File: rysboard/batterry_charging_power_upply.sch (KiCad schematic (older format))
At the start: 28 parts, among them J20 Conn_01x02, Q5 DMP3036SSD-13, Q6 DMP3036SSD-13, Q7 NST847BDP6T5G, Q9 Si7938DP-T1-GE3, U12 LTC4007

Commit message: more work done
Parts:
- removed C37, C40, C41, C42: C, symbol Device:C
- removed Q7: NST847BDP6T5G, Package_TO_SOT_SMD:SOT-963, symbol rysboard:NST847BDP6T5G
- removed R47, R48: R, symbol Device:R
- added C?: 15nF, Capacitor_SMD:C_0603_1608Metric, symbol Device:C
- added C? (x3): 10uF, Capacitor_SMD:C_1206_3216Metric, symbol Device:C
- added Q15: NST847BDP6T5G, Package_TO_SOT_SMD:SOT-963, symbol rysboard:DMP3036SSD-13
- added Q16: NST847BDP6T5G, Package_TO_SOT_SMD:SOT-963, symbol rysboard:NST847BDP6T5G
- added R41: 10KR, Resistor_SMD:R_0603_1608Metric_Pad1.05x0.95mm_HandSolder, symbol Device:R
- added R72: 10KR, Resistor_SMD:R_0603_1608Metric, symbol Device:R
- added R?: 26,7KR1%, Resistor_SMD:R_0603_1608Metric, symbol Device:R
- added R?: 25mR0.5%, symbol Device:R
- C35: value C -> 0.1uF; footprint (none) -> Capacitor_SMD:C_0603_1608Metric
- C38: value C -> 4,7nF; footprint (none) -> Capacitor_SMD:C_0603_1608Metric_Pad1.05x0.95mm_HandSolder
- C39: value C -> 10uF; footprint (none) -> Capacitor_SMD:C_1206_3216Metric
- L2: value INDUCTOR -> 10uH
- R39: value R -> 10KR; footprint (none) -> Resistor_SMD:R_0603_1608Metric_Pad1.05x0.95mm_HandSolder
- R42: value R -> 300KR; footprint (none) -> Resistor_SMD:R_0603_1608Metric_Pad1.05x0.95mm_HandSolder
- R46: value R -> 5KR; footprint (none) -> Resistor_SMD:R_0603_1608Metric_Pad1.05x0.95mm_HandSolder
- R49: value R -> 25mR0.5%
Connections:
- net +12V: now also C?.2, C?.2, C?.2, R?.1; no longer Q6.7 (d), Q6.8 (d), R46.1
- net +24V: now also Q15.1 (S1), R41.1; no longer C35.1, Q6.1 (S1), U12.1 (DCIN)
- net +BATT: now also C?.1
- net GND: now also C?.1, C?.1, C?.2, Q16.1 (E1), Q16.4 (E2), R?.1
- net current_monitor: now also R?.2
- net at R46.2, U12.18 (CLP): now also C?.1
- net at U12.24 (SHDN): now also Q16.3 (C2)
- net at R40.1: now also Q16.2 (B1)
- new net: C35.1, Q15.7 (d), Q15.8 (d), Q6.7 (d), Q6.8 (d), U12.1 (DCIN)
- new net: Q6.1 (S1), R46.1, R?.2
- new net: Q15.2 (G1), Q16.6 (C1), R41.2
- new net: Q16.5 (B2), R72.2
- new net ENABLE_CHARGING: R72.1
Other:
- note added: "SETUP FOR 4A"
- note added: "~2 Hours charging time"
- moved on the sheet: R40, R44

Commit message: more footprints
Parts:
- C34, C36: footprint (none) -> Capacitor_SMD:C_0603_1608Metric
- gave numbers to parts that had none: 6
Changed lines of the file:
@@
 F 0 "C36" H 6415 3646 50  0000 L CNN
 F 1 "C" H 6415 3555 50  0000 L CNN
-F 2 "" H 6338 3450 50  0001 C CNN
+F 2 "Capacitor_SMD:C_0603_1608Metric" H 6338 3450 50  0001 C CNN
 F 3 "~" H 6300 3600 50  0001 C CNN
 	1    6300 3600
@@
 F 0 "C34" H 2450 2400 50  0000 L CNN
 F 1 "C" H 2450 2250 50  0000 L CNN
-F 2 "" H 2638 2150 50  0001 C CNN
+F 2 "Capacitor_SMD:C_0603_1608Metric" H 2638 2150 50  0001 C CNN
 F 3 "~" H 2600 2300 50  0001 C CNN
 	1    2600 2300
@@
 Connection ~ 3650 2050
 $Comp
-L Device:C C?
+L Device:C C37
 U 1 1 6048E11B
 P 6850 2050
-F 0 "C?" H 6965 2096 50  0000 L CNN
+F 0 "C37" H 6965 2096 50  0000 L CNN
 F 1 "15nF" H 6965 2005 50  0000 L CNN
 F 2 "Capacitor_SMD:C_0603_1608Metric" H 6888 1900 50  0001 C CNN
@@
 	6850 2200 7550 2200
 $Comp
-L Device:C C?
+L Device:C C42
 U 1 1 6048ED93
 P 9650 2900
-F 0 "C?" H 9765 2946 50  0000 L CNN
+F 0 "C42" H 9765 2946 50  0000 L CNN
 F 1 "10uF" H 9765 2855 50  0000 L CNN
 F 2 "Capacitor_SMD:C_1206_3216Metric" H 9688 2750 50  0001 C CNN
@@
 ~2 Hours charging time
 $Comp
-L Device:R R?
+L Device:R R48
 U 1 1 6049324E
 P 7575 3600
-F 0 "R?" H 7575 3600 50  0000 C CNN
+F 0 "R48" H 7575 3600 50  0000 C CNN
 F 1 "26,7KR1%" H 7575 3800 50  0000 C CNN
 F 2 "Resistor_SMD:R_0603_1608Metric" V 7505 3600 50  0001 C CNN
@@
 	7575 3450 8325 3450
 $Comp
-L Device:R R?
+L Device:R R47
 U 1 1 604A0F07
 P 7550 2050
-F 0 "R?" H 7300 2000 50  0000 C CNN
+F 0 "R47" H 7300 2000 50  0000 C CNN
 F 1 "25mR0.5%" H 7275 1925 50  0000 C CNN
 F 2 "" V 7480 2050 50  0001 C CNN
@@
 Connection ~ 7550 1900
 $Comp
-L Device:C C?
+L Device:C C40
 U 1 1 604CA4CA
 P 8275 2050
-F 0 "C?" H 8390 2096 50  0000 L CNN
+F 0 "C40" H 8390 2096 50  0000 L CNN
 F 1 "10uF" H 8390 2005 50  0000 L CNN
 F 2 "Capacitor_SMD:C_1206_3216Metric" H 8313 1900 50  0001 C CNN
@@
 $EndComp
 $Comp
-L Device:C C?
+L Device:C C41
 U 1 1 604CA7A0
 P 8700 2050
-F 0 "C?" H 8815 2096 50  0000 L CNN
+F 0 "C41" H 8815 2096 50  0000 L CNN
 F 1 "10uF" H 8815 2005 50  0000 L CNN
 F 2 "Capacitor_SMD:C_1206_3216Metric" H 8738 1900 50  0001 C CNN
@@
 	9175 2200 9925 2200
 $Comp
-L power:GND #PWR?
+L power:GND #PWR0106
 U 1 1 604CDA85
 P 8700 1900
-F 0 "#PWR?" H 8700 1650 50  0001 C CNN
+F 0 "#PWR0106" H 8700 1650 50  0001 C CNN
 F 1 "GND" H 8705 1727 50  0000 C CNN
 F 2 "" H 8700 1900 50  0001 C CNN
@@
 $EndComp
 $Comp
-L power:GND #PWR?
+L power:GND #PWR0107
 U 1 1 604CE081
 P 8275 1900
-F 0 "#PWR?" H 8275 1650 50  0001 C CNN
+F 0 "#PWR0107" H 8275 1650 50  0001 C CNN
 F 1 "GND" H 8280 1727 50  0000 C CNN
 F 2 "" H 8275 1900 50  0001 C CNN

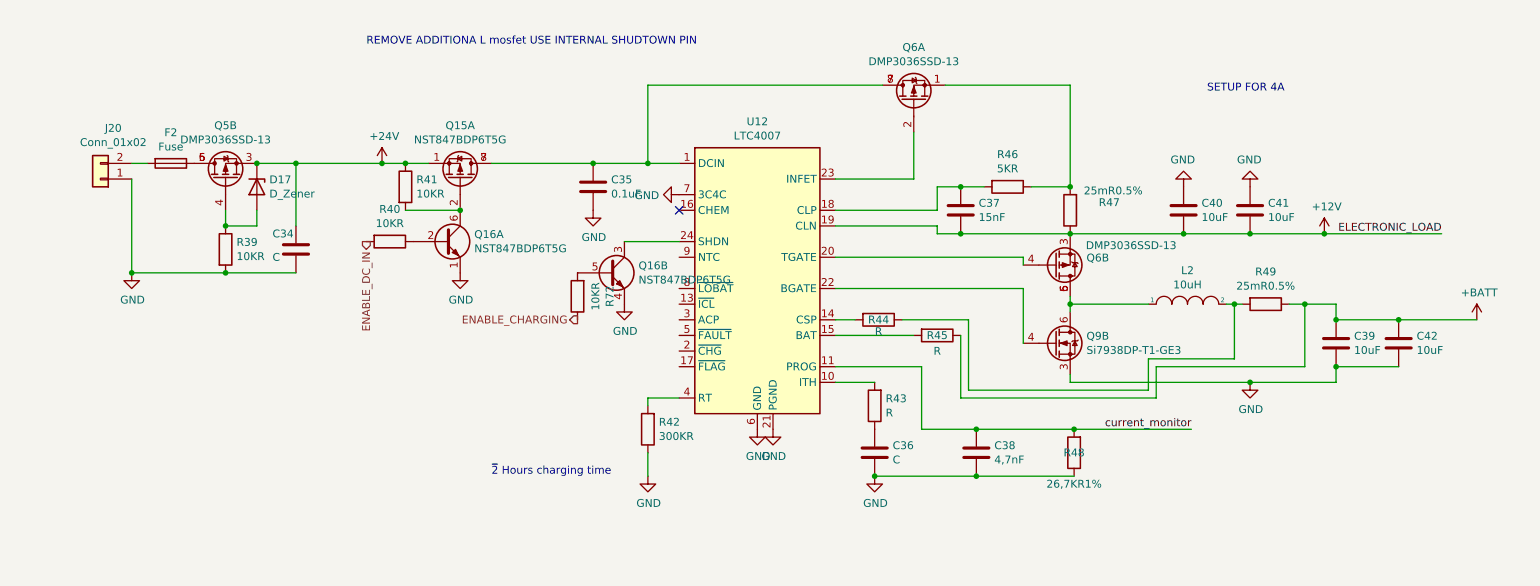
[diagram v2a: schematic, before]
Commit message: ltc4007 configured
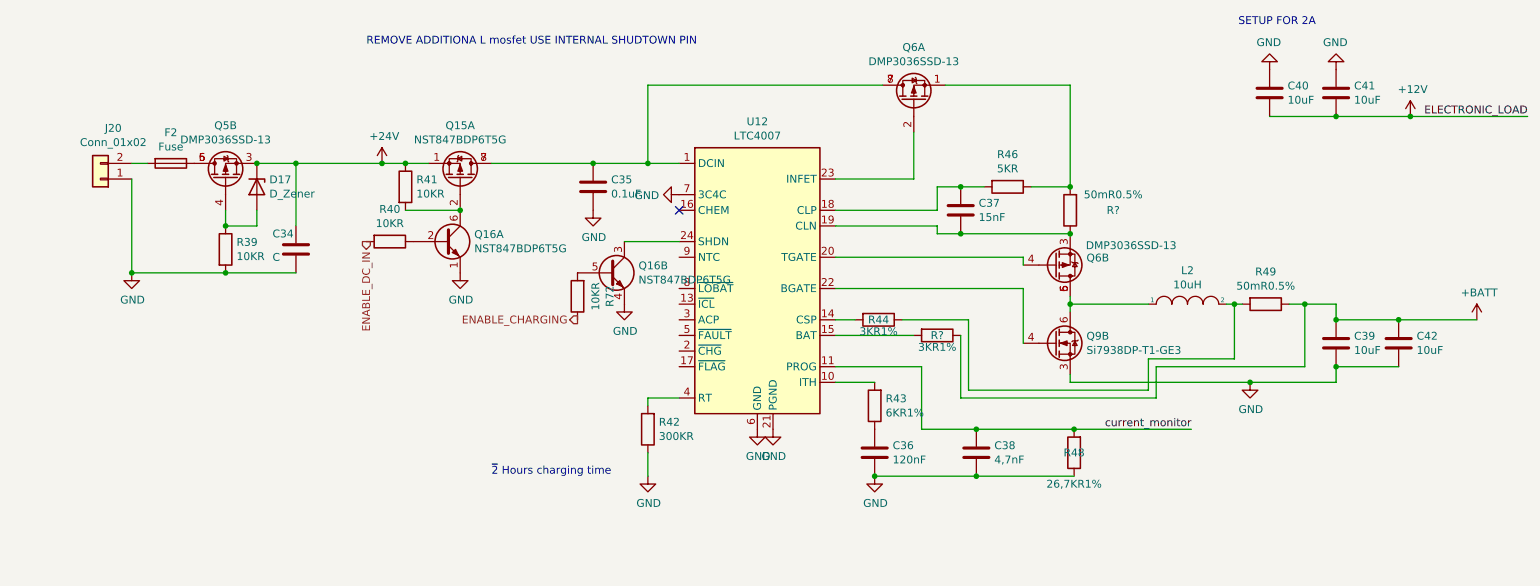
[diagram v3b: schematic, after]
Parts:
- removed R45: R, symbol Device:R
- removed R47: 25mR0.5%, symbol Device:R
- added R?: 3KR1%, Resistor_SMD:R_0603_1608Metric, symbol Device:R
- added R?: 50mR0.5%, symbol Device:R
- C36: value C -> 120nF
- R43: value R -> 6KR1%; footprint (none) -> Resistor_SMD:R_0603_1608Metric
- R44: value R -> 3KR1%; footprint (none) -> Resistor_SMD:R_0603_1608Metric
- R49: value 25mR0.5% -> 50mR0.5%
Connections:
- net +12V: no longer C37.2, Q6.3 (S2), U12.19 (CLN)
- net +BATT: now also R?.1
- net at U12.15 (BAT): now also R?.2
- net at Q6.1 (S1), R46.1: now also R?.2
- new net: C37.2, Q6.3 (S2), R?.1, U12.19 (CLN)
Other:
- note added: "SETUP FOR 2A"
- note removed: "SETUP FOR 4A"
- moved on the sheet: C40, C41

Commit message: LTC4007 done
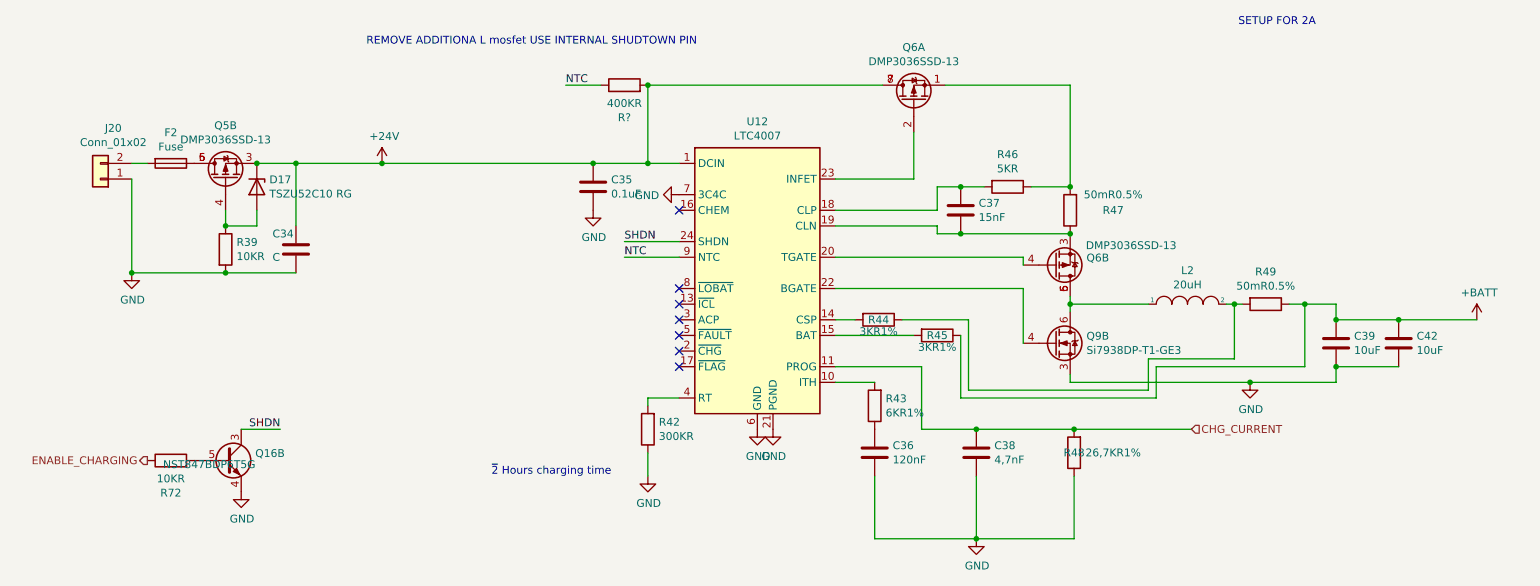
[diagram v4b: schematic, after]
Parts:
- removed C40, C41: 10uF, Capacitor_SMD:C_1206_3216Metric, symbol Device:C
- removed Q15: NST847BDP6T5G, Package_TO_SOT_SMD:SOT-963, symbol rysboard:DMP3036SSD-13
- removed unit 1 of Q16
- removed R40: 10KR, Resistor_SMD:R_0603_1608Metric, symbol Device:R
- removed R41: 10KR, Resistor_SMD:R_0603_1608Metric_Pad1.05x0.95mm_HandSolder, symbol Device:R
- added R?: 400KR, Resistor_SMD:R_0603_1608Metric, symbol Device:R
- D17: value D_Zener -> TSZU52C10 RG; footprint (none) -> Diode_SMD:D_0603_1608Metric
- F2: footprint (none) -> Fuse:Fuse_1206_3216Metric
- L2: value 10uH -> 20uH
- gave numbers to parts that had none: 2
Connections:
- net +24V: now also C35.1, Q6.7 (d), Q6.8 (d), U12.1 (DCIN), R?.2
- net SHDN: now reaches Q16.3 (C2), U12.24 (SHDN)
- net NTC: now reaches U12.9 (NTC)
- net NTC: now also R?.1
- net current_monitor renamed CHG_CURRENT
- no-connect marks 1 -> 7
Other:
- moved on the sheet: Q16B, R72
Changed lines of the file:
@@
 P 2350 1900
 F 0 "D17" V 2304 1980 50  0000 L CNN
-F 1 "D_Zener" V 2395 1980 50  0000 L CNN
-F 2 "" H 2350 1900 50  0001 C CNN
+F 1 "TSZU52C10 RG" V 2395 1980 50  0000 L CNN
+F 2 "Diode_SMD:D_0603_1608Metric" H 2350 1900 50  0001 C CNN
 F 3 "~" H 2350 1900 50  0001 C CNN
 	1    2350 1900
@@
 F 0 "F2" V 1603 1750 50  0000 C CNN
 F 1 "Fuse" V 1694 1750 50  0000 C CNN
-F 2 "" V 1730 1750 50  0001 C CNN
+F 2 "Fuse:Fuse_1206_3216Metric" V 1730 1750 50  0001 C CNN
 F 3 "~" H 1800 1750 50  0001 C CNN
 	1    1800 1750
@@
 P 8300 2650
 F 0 "L2" H 8300 2865 50  0000 C CNN
-F 1 "10uH" H 8300 2774 50  0000 C CNN
+F 1 "20uH" H 8300 2774 50  0000 C CNN
 F 2 "" H 8300 2650 50  0001 C CNN
 F 3 "~" H 8300 2650 50  0001 C CNN
@@
 $EndComp
 Wire Wire Line
-	6300 3750 6950 3750
-Connection ~ 6950 3750
-Wire Wire Line
 	6300 3150 6050 3150
 $Comp
 L power:GND #PWR046
 U 1 1 5FF27CDA
-P 6300 3750
-F 0 "#PWR046" H 6300 3500 50  0001 C CNN
-F 1 "GND" H 6305 3577 50  0000 C CNN
-F 2 "" H 6300 3750 50  0001 C CNN
-F 3 "" H 6300 3750 50  0001 C CNN
-	1    6300 3750
-	1    0    0    -1
-$EndComp
-Connection ~ 6300 3750
-Text Label 8325 3450 2    50   ~ 0
-current_monitor
-Text Label 10475 1450 2    50   ~ 0
-ELECTRONIC_LOAD
+P 6950 4150
+F 0 "#PWR046" H 6950 3900 50  0001 C CNN
+F 1 "GND" H 6955 3977 50  0000 C CNN
+F 2 "" H 6950 4150 50  0001 C CNN
+F 3 "" H 6950 4150 50  0001 C CNN
+	1    6950 4150
+	1    0    0    -1
+$EndComp
 $Comp
 L Device:R R42
@@
 REMOVE ADDITIONA L mosfet USE INTERNAL SHUDTOWN PIN
 $Comp
-L power:+12V #PWR061
-U 1 1 604387DC
-P 9725 1450
-F 0 "#PWR061" H 9725 1300 50  0001 C CNN
-F 1 "+12V" H 9740 1623 50  0000 C CNN
-F 2 "" H 9725 1450 50  0001 C CNN
-F 3 "" H 9725 1450 50  0001 C CNN
-	1    9725 1450
-	1    0    0    -1
-$EndComp
-$Comp
 L rysboard:DMP3036SSD-13 Q5
 U 2 1 6050A980
@@
 L Device:R R72
 U 1 1 6047C363
-P 4400 2600
-F 0 "R72" V 4193 2600 50  0000 C CNN
-F 1 "10KR" V 4284 2600 50  0000 C CNN
-F 2 "Resistor_SMD:R_0603_1608Metric" V 4330 2600 50  0001 C CNN
-F 3 "~" H 4400 2600 50  0001 C CNN
-	1    4400 2600
-	-1   0    0    1
+P 1800 3650
+F 0 "R72" V 1593 3650 50  0000 C CNN
+F 1 "10KR" V 1684 3650 50  0000 C CNN
+F 2 "Resistor_SMD:R_0603_1608Metric" V 1730 3650 50  0001 C CNN
+F 3 "~" H 1800 3650 50  0001 C CNN
+	1    1800 3650
+	0    -1   -1   0
 $EndComp
 $Comp
 L power:GND #PWR065
 U 1 1 6047C8D4
-P 4700 2650
-F 0 "#PWR065" H 4700 2400 50  0001 C CNN
-F 1 "GND" H 4705 2477 50  0000 C CNN
-F 2 "" H 4700 2650 50  0001 C CNN
-F 3 "" H 4700 2650 50  0001 C CNN
-	1    4700 2650
-	1    0    0    -1
-$EndComp
-Text HLabel 4400 2750 0    50   Output ~ 0
+P 2250 3850
+F 0 "#PWR065" H 2250 3600 50  0001 C CNN
+F 1 "GND" H 2255 3677 50  0000 C CNN
+F 2 "" H 2250 3850 50  0001 C CNN
+F 3 "" H 2250 3850 50  0001 C CNN
+	1    2250 3850
+	1    0    0    -1
+$EndComp
+Text HLabel 1650 3650 0    50   Output ~ 0
 ENABLE_CHARGING
 $Comp
 L rysboard:NST847BDP6T5G Q16
 U 2 1 6047E1C9
-P 4600 2450
-F 0 "Q16" H 4790 2496 50  0000 L CNN
-F 1 "NST847BDP6T5G" H 4790 2405 50  0000 L CNN
-F 2 "Package_TO_SOT_SMD:SOT-963" H 4800 2550 50  0001 C CNN
-F 3 "~" H 4600 2450 50  0001 C CNN
-	2    4600 2450
+P 2150 3650
+F 0 "Q16" H 2340 3696 50  0000 L CNN
+F 1 "NST847BDP6T5G" H 1750 3625 50  0000 L CNN
+F 2 "Package_TO_SOT_SMD:SOT-963" H 2350 3750 50  0001 C CNN
+F 3 "~" H 2150 3650 50  0001 C CNN
+	2    2150 3650
 	1    0    0    -1
 $EndComp
@@
 P 7575 3600
 F 0 "R48" H 7575 3600 50  0000 C CNN
-F 1 "26,7KR1%" H 7575 3800 50  0000 C CNN
+F 1 "26,7KR1%" H 7325 3600 50  0000 C CNN
 F 2 "Resistor_SMD:R_0603_1608Metric" V 7505 3600 50  0001 C CNN
 F 3 "~" H 7575 3600 50  0001 C CNN
@@
 $EndComp
 Wire Wire Line
-	6950 3750 7575 3750
-Wire Wire Line
 	6950 3450 7575 3450
 Connection ~ 7575 3450
 Wire Wire Line
 	7575 3450 8325 3450
-$Comp
-L Device:C C40
-U 1 1 604CA4CA
-P 8825 1300
-F 0 "C40" H 8940 1346 50  0000 L CNN
-F 1 "10uF" H 8940 1255 50  0000 L CNN
-F 2 "Capacitor_SMD:C_1206_3216Metric" H 8863 1150 50  0001 C CNN
-F 3 "~" H 8825 1300 50  0001 C CNN
-	1    8825 1300
-	1    0    0    -1
-$EndComp
-$Comp
-L Device:C C41
-U 1 1 604CA7A0
-P 9250 1300
-F 0 "C41" H 9365 1346 50  0000 L CNN
-F 1 "10uF" H 9365 1255 50  0000 L CNN
-F 2 "Capacitor_SMD:C_1206_3216Metric" H 9288 1150 50  0001 C CNN
-F 3 "~" H 9250 1300 50  0001 C CNN
-	1    9250 1300
-	1    0    0    -1
-$EndComp
-Wire Wire Line
-	8825 1450 9250 1450
-Connection ~ 9250 1450
-Wire Wire Line
-	9250 1450 9725 1450
-Connection ~ 9725 1450
-Wire Wire Line
-	9725 1450 10475 1450
-$Comp
-L power:GND #PWR0106
-U 1 1 604CDA85
-P 9250 1150
-F 0 "#PWR0106" H 9250 900 50  0001 C CNN
-F 1 "GND" H 9255 977 50  0000 C CNN
-F 2 "" H 9250 1150 50  0001 C CNN
-F 3 "" H 9250 1150 50  0001 C CNN
-	1    9250 1150
-	-1   0    0    1
-$EndComp
-$Comp
-L power:GND #PWR0107
-U 1 1 604CE081
-P 8825 1150
-F 0 "#PWR0107" H 8825 900 50  0001 C CNN
-F 1 "GND" H 8830 977 50  0000 C CNN
-F 2 "" H 8825 1150 50  0001 C CNN
-F 3 "" H 8825 1150 50  0001 C CNN
-	1    8825 1150
-	-1   0    0    1
-$EndComp
 Text Notes 8625 875  0    50   ~ 0
 SETUP FOR 2A
 $Comp
-L Device:R R?
+L Device:R R45
 U 1 1 60466C52
 P 6700 2850
-F 0 "R?" V 6700 2850 50  0000 C CNN
+F 0 "R45" V 6700 2850 50  0000 C CNN
 F 1 "3KR1%" V 6775 2850 50  0000 C CNN
 F 2 "Resistor_SMD:R_0603_1608Metric" V 6630 2850 50  0001 C CNN
@@
 Connection ~ 7550 2200
 Connection ~ 7550 1900
-Wire Wire Line
-	3850 1750 4500 1750
-Connection ~ 3300 1750
-Wire Wire Line
-	3300 1750 3450 1750
-Wire Wire Line
-	3150 1750 3300 1750
-Connection ~ 3650 2050
-$Comp
-L rysboard:NST847BDP6T5G Q16
-U 1 1 6047DFC9
-P 3550 2250
-F 0 "Q16" H 3740 2296 50  0000 L CNN
-F 1 "NST847BDP6T5G" H 3740 2205 50  0000 L CNN
-F 2 "Package_TO_SOT_SMD:SOT-963" H 3750 2350 50  0001 C CNN
-F 3 "~" H 3550 2250 50  0001 C CNN
-	1    3550 2250
-	1    0    0    -1
-$EndComp
-Wire Wire Line
-	3300 2050 3650 2050
-$Comp
-L Device:R R41
-U 1 1 6047643D
-P 3300 1900
-F 0 "R41" H 3370 1946 50  0000 L CNN
-F 1 "10KR" H 3370 1855 50  0000 L CNN
-F 2 "Resistor_SMD:R_0603_1608Metric_Pad1.05x0.95mm_HandSolder" V 3230 1900 50  0001 C CNN
-F 3 "~" H 3300 1900 50  0001 C CNN
-	1    3300 1900
-	1    0    0    -1
-$EndComp
-$Comp
-L rysboard:DMP3036SSD-13 Q15
-U 1 1 60470445
-P 3650 1850
-F 0 "Q15" V 3992 1850 50  0000 C CNN
-F 1 "NST847BDP6T5G" V 3901 1850 50  0000 C CNN
-F 2 "Package_TO_SOT_SMD:SOT-963" H 3850 1775 50  0001 L CIN
-F 3 "~" H 3650 1850 50  0001 L CNN
-	1    3650 1850
-	0    1    -1   0
-$EndComp
-Text HLabel 3050 2250 3    50   Output ~ 0
-ENABLE_DC_IN
-$Comp
-L Device:R R40
-U 1 1 606AC756
-P 3200 2250
-F 0 "R40" V 2993 2250 50  0000 C CNN
-F 1 "10KR" V 3084 2250 50  0000 C CNN
-F 2 "Resistor_SMD:R_0603_1608Metric" V 3130 2250 50  0001 C CNN
-F 3 "~" H 3200 2250 50  0001 C CNN
-	1    3200 2250
-	0    1    1    0
-$EndComp
-$Comp
-L power:GND #PWR041
-U 1 1 606AC403
-P 3650 2450
-F 0 "#PWR041" H 3650 2200 50  0001 C CNN
-F 1 "GND" H 3655 2277 50  0000 C CNN
-F 2 "" H 3650 2450 50  0001 C CNN
-F 3 "" H 3650 2450 50  0001 C CNN
-	1    3650 2450
-	1    0    0    -1
-$EndComp
-$Comp
-L Device:R R?
+$Comp
+L Device:R R47
 U 1 1 6046F89B
 P 7550 2050
-F 0 "R?" H 7275 2050 50  0000 C CNN
+F 0 "R47" H 7275 2050 50  0000 C CNN
 F 1 "50mR0.5%" H 7275 1950 50  0000 C CNN
 F 2 "" V 7480 2050 50  0001 C CNN
@@
 	-1   0    0    1
 $EndComp
+Wire Wire Line
+	6300 4150 6300 3750
+Connection ~ 6950 4150
+Wire Wire Line
+	6950 4150 6300 4150
+Wire Wire Line
+	6950 3750 6950 4150
+Wire Wire Line
+	7575 4150 6950 4150
+Text HLabel 8325 3450 2    50   Input ~ 0
+CHG_CURRENT
+Wire Wire Line
+	7575 3750 7575 4150
+NoConn ~ 5050 2550
+NoConn ~ 5050 2650
+NoConn ~ 5050 2750
+NoConn ~ 5050 2850
+NoConn ~ 5050 2950
+NoConn ~ 5050 3050
+$Comp
+L Device:R R?
+U 1 1 604ECFAE
+P 4700 1250
+F 0 "R?" V 4493 1250 50  0000 C CNN
+F 1 "400KR" V 4584 1250 50  0000 C CNN
+F 2 "Resistor_SMD:R_0603_1608Metric" V 4630 1250 50  0001 C CNN
+F 3 "~" H 4700 1250 50  0001 C CNN
+	1    4700 1250
+	0    -1   -1   0
+$EndComp
+Text Label 4700 2250 0    50   ~ 0
+SHDN
+Text Label 4700 2350 0    50   ~ 0
+NTC
+Wire Wire Line
+	5050 2350 4700 2350
+Text Label 2500 3450 2    50   ~ 0
+SHDN
+Wire Wire Line
+	2500 3450 2250 3450
+Connection ~ 4850 1250
+Text Label 4325 1250 0    50   ~ 0
+NTC
+Wire Wire Line
+	4325 1250 4550 1250
+Wire Wire Line
+	3150 1750 4500 1750
 $EndSCHEMATC

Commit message: Even More footprints
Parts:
- R47, R49: footprint (none) -> Resistor_SMD:R_1206_3216Metric
- gave numbers to parts that had none: 1
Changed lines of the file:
@@
 F 0 "R49" V 8593 2650 50  0000 C CNN
 F 1 "50mR0.5%" V 8684 2650 50  0000 C CNN
-F 2 "" V 8730 2650 50  0001 C CNN
+F 2 "Resistor_SMD:R_1206_3216Metric" V 8730 2650 50  0001 C CNN
 F 3 "~" H 8800 2650 50  0001 C CNN
 	1    8800 2650
@@
 F 0 "R47" H 7275 2050 50  0000 C CNN
 F 1 "50mR0.5%" H 7275 1950 50  0000 C CNN
-F 2 "" V 7480 2050 50  0001 C CNN
+F 2 "Resistor_SMD:R_1206_3216Metric" V 7480 2050 50  0001 C CNN
 F 3 "~" H 7550 2050 50  0001 C CNN
 	1    7550 2050
@@
 NoConn ~ 5050 3050
 $Comp
-L Device:R R?
+L Device:R R41
 U 1 1 604ECFAE
 P 4700 1250
-F 0 "R?" V 4493 1250 50  0000 C CNN
+F 0 "R41" V 4493 1250 50  0000 C CNN
 F 1 "400KR" V 4584 1250 50  0000 C CNN
 F 2 "Resistor_SMD:R_0603_1608Metric" V 4630 1250 50  0001 C CNN

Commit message: More Work. RPI can now programm STM32 via GPIO
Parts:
- L2: value 20uH -> 22uH; footprint (none) -> Inductor_SMD:L_10.4x10.4_H4.8
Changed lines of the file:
@@
 P 8300 2650
 F 0 "L2" H 8300 2865 50  0000 C CNN
-F 1 "20uH" H 8300 2774 50  0000 C CNN
-F 2 "" H 8300 2650 50  0001 C CNN
+F 1 "22uH" H 8300 2774 50  0000 C CNN
+F 2 "Inductor_SMD:L_10.4x10.4_H4.8" H 8300 2650 50  0001 C CNN
 F 3 "~" H 8300 2650 50  0001 C CNN
 	1    8300 2650
